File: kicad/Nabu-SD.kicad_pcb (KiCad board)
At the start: 2 copper layers, 127 x 53.2 mm, 73 parts, among them J1 Nabu Expansion Slot, J10 USB_B_Micro, J2 ICSP, J3 SD Card, J4 Serial, J5 I2C, J6 OUT1, J7 SD Card, J8A1 XKTF-005, J8B1 XKTF-0803-0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

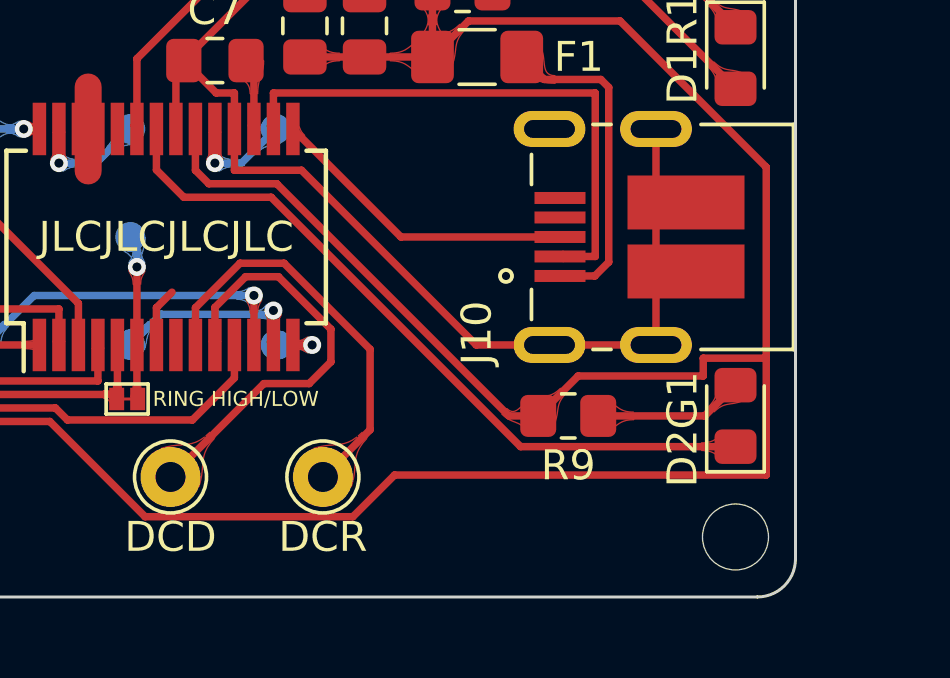
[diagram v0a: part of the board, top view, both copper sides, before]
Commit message: Rotate Green LED 180 degrees on Serial breakout.
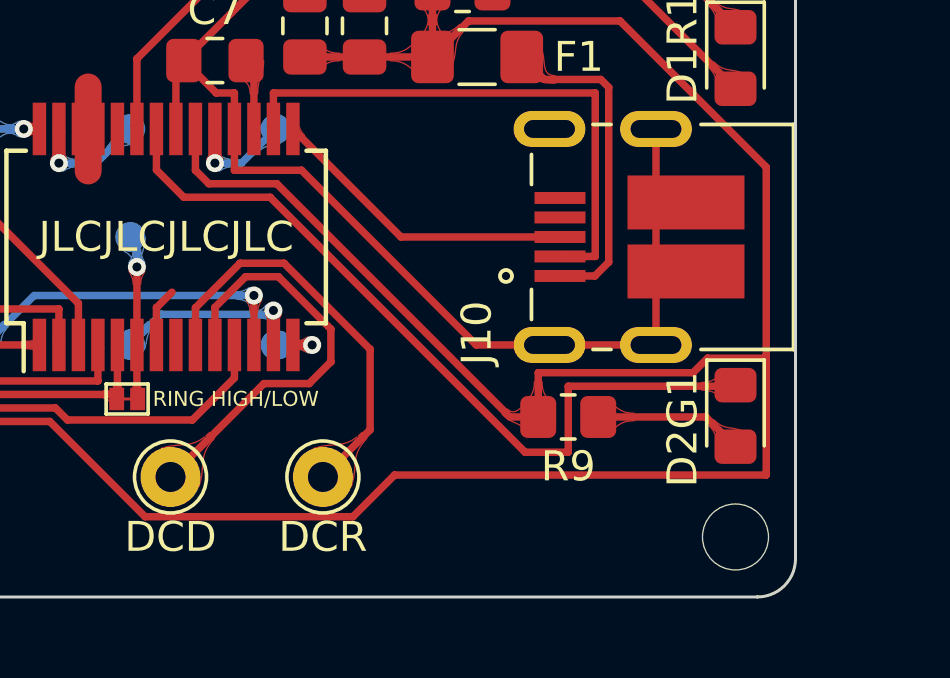
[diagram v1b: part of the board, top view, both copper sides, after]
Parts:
- turned D2G1 to -90 degrees
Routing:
- net /Serial_Breakout/RXLED_GRN: track 24.5 -> 26.8 mm
- net +5VD: track 124.2 -> 124.8 mm
